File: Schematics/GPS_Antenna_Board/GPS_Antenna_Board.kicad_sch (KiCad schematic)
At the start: 26 parts, among them J1 470804001, U3 SAM-M10Q, U8 LM66100DCKR

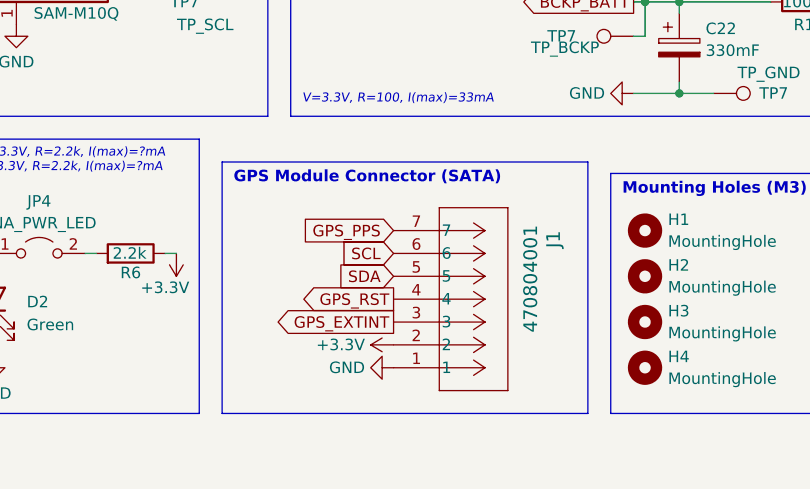
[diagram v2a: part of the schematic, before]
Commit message: Verified part numbers & made ERC pass
Also cleaned up unnecessary footprints & added bulk filtering capacitor to GPS antenna board
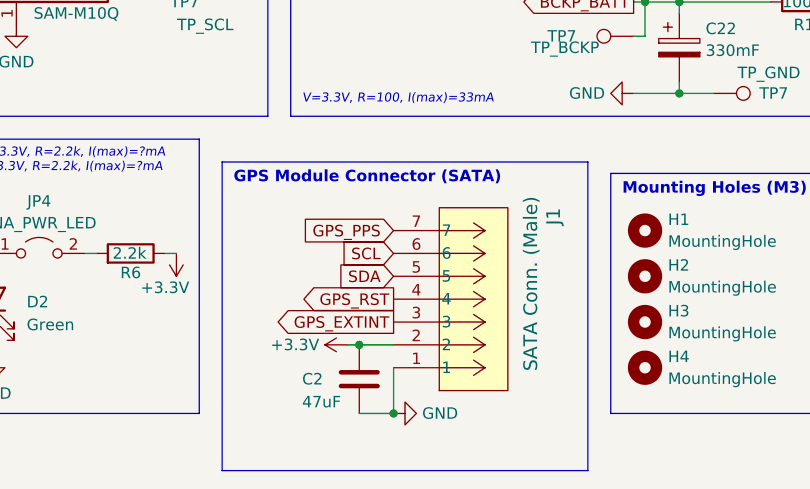
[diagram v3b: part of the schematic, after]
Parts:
- added C2: 47uF, Capacitor_SMD:C_0805_2012Metric, symbol Device:C
- J1: value 470804001 -> SATA Conn. (Male); footprint footprints:CONN_47080-4001_MOL_SATA -> CONN_47080-4001_MOL
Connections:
- net +3.3V: now also C2.1
- net GND: now also C2.2
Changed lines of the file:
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@@
   (junction (at 119.38 62.23) (diameter 0) (color 0 0 0 0)
   )
+  (junction (at 154.94 125.73) (diameter 0) (color 0 0 0 0)
+  )
   (junction (at 99.06 77.47) (diameter 0) (color 0 0 0 0)
   )
@@
   )
   (junction (at 186.69 87.63) (diameter 0) (color 0 0 0 0)
+  )
+  (junction (at 158.75 133.35) (diameter 0) (color 0 0 0 0)
   )
   (junction (at 134.62 80.01) (diameter 0) (color 0 0 0 0)
@@
     (stroke (width 0) (type default))
   )
+  (wire (pts (xy 158.75 128.27) (xy 158.75 133.35))
+    (stroke (width 0) (type default))
+  )
   (wire (pts (xy 119.38 55.88) (xy 119.38 62.23))
     (stroke (width 0) (type default))
@@
     (stroke (width 0) (type default))
   )
+  (wire (pts (xy 153.67 125.73) (xy 154.94 125.73))
+    (stroke (width 0) (type default))
+  )
   (wire (pts (xy 186.69 91.44) (xy 186.69 87.63))
     (stroke (width 0) (type default))
@@
     (stroke (width 0) (type default))
   )
+  (wire (pts (xy 154.94 125.73) (xy 158.75 125.73))
+    (stroke (width 0) (type default))
+  )
   (wire (pts (xy 129.54 82.55) (xy 134.62 82.55))
     (stroke (width 0) (type default))
@@
     (stroke (width 0) (type default))
   )
+  (wire (pts (xy 154.94 133.35) (xy 158.75 133.35))
+    (stroke (width 0) (type default))
+  )
   (wire (pts (xy 162.56 76.2) (xy 165.1 76.2))
     (stroke (width 0) (type default))
@@
     (fill (type none))
   )
-  (rectangle (start 139.7 105.41) (end 180.34 133.35)
+  (rectangle (start 139.7 105.41) (end 180.34 139.7)
     (stroke (width 0) (type default))
     (fill (type none))
@@
       (effects (font (size 1.27 1.27) italic) hide)
     )
-    (property "Datasheet" "https://www.ti.com/general/docs/suppproductinfo.tsp?distId=10&gotoUrl=https%3A%2F%2Fwww.ti.com%2Flit%2Fgpn%2flm66100" (at 185.42 74.93 0)
+    (property "Datasheet" "" (at 185.42 74.93 0)
       (effects (font (size 1.27 1.27) italic) hide)
     )
@@
     )
   )
-  (symbol (lib_id "power:+3.3V") (at 158.75 125.73 90) (unit 1)
+  (symbol (lib_id "power:+3.3V") (at 153.67 125.73 90) (unit 1)
     (in_bom yes) (on_board yes) (dnp no) (fields_autoplaced)
-    (property "Reference" "#PWR02" (at 162.56 125.73 0)
-      (effects (font (size 1.27 1.27)) hide)
-    )
-    (property "Value" "+3.3V" (at 155.575 125.73 90)
-      (effects (font (size 1.27 1.27)) (justify left))
-    )
-    (property "Footprint" "" (at 158.75 125.73 0)
-      (effects (font (size 1.27 1.27)) hide)
-    )
-    (property "Datasheet" "" (at 158.75 125.73 0)
+    (property "Reference" "#PWR02" (at 157.48 125.73 0)
+      (effects (font (size 1.27 1.27)) hide)
+    )
+    (property "Value" "+3.3V" (at 150.495 125.73 90)
+      (effects (font (size 1.27 1.27)) (justify left))
+    )
+    (property "Footprint" "" (at 153.67 125.73 0)
+      (effects (font (size 1.27 1.27)) hide)
+    )
+    (property "Datasheet" "" (at 153.67 125.73 0)
       (effects (font (size 1.27 1.27)) hide)
     )
@@
   (symbol (lib_id "CONN_47080-4001_MOL_SATA:470804001") (at 158.75 128.27 0) (mirror x) (unit 1)
     (in_bom yes) (on_board yes) (dnp no)
-    (property "Reference" "J1" (at 176.53 113.03 90)
+    (property "Reference" "J1" (at 176.53 110.49 90)
       (effects (font (size 1.524 1.524)) (justify left))
     )
-    (property "Value" "470804001" (at 173.99 112.395 90)
+    (property "Value" "SATA Conn. (Male)" (at 173.99 109.22 90)
       (effects (font (size 1.524 1.524)) (justify left))
     )
-    (property "Footprint" "footprints:CONN_47080-4001_MOL_SATA" (at 158.75 128.27 0)
+    (property "Footprint" "CONN_47080-4001_MOL" (at 158.75 128.27 0)
       (effects (font (size 1.27 1.27) italic) hide)
     )
@@
     )
   )
-  (symbol (lib_id "power:GND") (at 158.75 128.27 270) (unit 1)
+  (symbol (lib_id "power:GND") (at 158.75 133.35 90) (unit 1)
     (in_bom yes) (on_board yes) (dnp no) (fields_autoplaced)
-    (property "Reference" "#PWR01" (at 152.4 128.27 0)
-      (effects (font (size 1.27 1.27)) hide)
-    )
-    (property "Value" "GND" (at 155.5751 128.27 90)
+    (property "Reference" "#PWR01" (at 165.1 133.35 0)
+      (effects (font (size 1.27 1.27)) hide)
+    )
+    (property "Value" "GND" (at 161.925 133.35 90)
       (effects (font (size 1.27 1.27)) (justify right))
     )
-    (property "Footprint" "" (at 158.75 128.27 0)
-      (effects (font (size 1.27 1.27)) hide)
-    )
-    (property "Datasheet" "" (at 158.75 128.27 0)
+    (property "Footprint" "" (at 158.75 133.35 0)
+      (effects (font (size 1.27 1.27)) hide)
+    )
+    (property "Datasheet" "" (at 158.75 133.35 0)
       (effects (font (size 1.27 1.27)) hide)
     )
@@
         )
       )
+    )
+  )
+  (symbol (lib_id "Device:C") (at 154.94 129.54 0) (unit 1)
+    (in_bom yes) (on_board yes) (dnp no)
+    (property "Reference" "C2" (at 148.59 129.54 0)
+      (effects (font (size 1.27 1.27)) (justify left))
+    )
+    (property "Value" "47uF" (at 148.59 132.08 0)
+      (effects (font (size 1.27 1.27)) (justify left))
+    )
+    (property "Footprint" "Capacitor_SMD:C_0805_2012Metric" (at 155.9052 133.35 0)
+      (effects (font (size 1.27 1.27)) hide)
+    )
+    (property "Datasheet" "~" (at 154.94 129.54 0)
+      (effects (font (size 1.27 1.27)) hide)
+    )
+    (property "LCSC" "C16780" (at 151.511 129.54 90)
+      (effects (font (size 1.27 1.27)) hide)
+    )
+    (pin "1")
+    (pin "2")
+    (instances
+      (project "CANBUSALL"
+        (path "/93bab7a2-0f5f-4ce1-a774-248550723259"
+          (reference "C2") (unit 1)
+        )
+      )
+      (project "canbusv1"
+        (path "/acb9ae9d-257e-47aa-b94e-3fc0ebc9a75c"
+          (reference "C1") (unit 1)
+        )
+      )
+      (project "Communications_Module"
+        (path "/ace06731-9b48-45c3-868d-c65fed1a8f9b"
+          (reference "C19") (unit 1)
+        )
+      )
+      (project "GPS_Module"
+        (path "/c9a01778-8bed-4fe7-bd5a-975b80c0ed6a"
+          (reference "C12") (unit 1)
+        )
+      )
+      (project "GPS_Antenna_Board"
+        (path "/f34e830a-ca26-47f3-b516-e4270044d2c1"
+          (reference "C5") (unit 1)
+        )
+      )

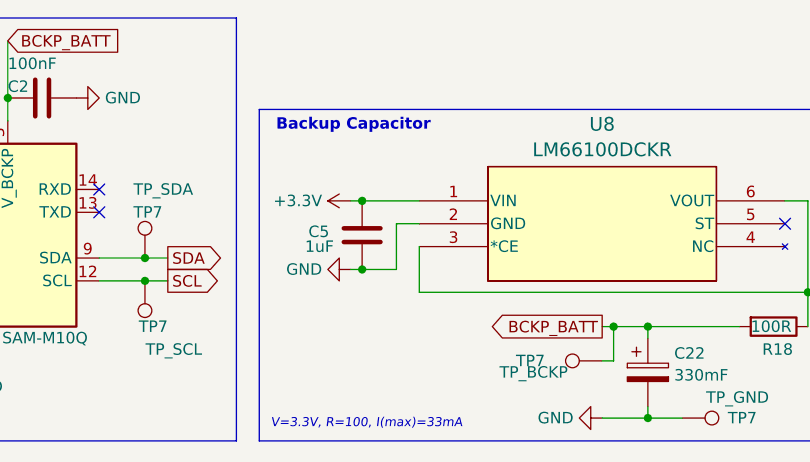
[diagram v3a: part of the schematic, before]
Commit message: Add silkscreen & final PCB adjustments
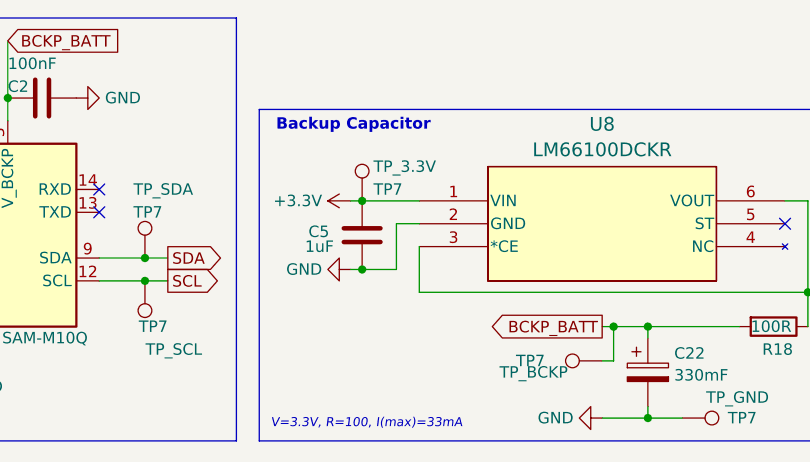
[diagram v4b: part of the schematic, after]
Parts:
- added TP7: TP_3.3V, TestPoint:TestPoint_Pad_1.5x1.5mm, symbol Connector:TestPoint
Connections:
- net +3.3V: now also TP7.1
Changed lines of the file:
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@@
+    )
+  )
+  (symbol (lib_id "Connector:TestPoint") (at 158.75 73.66 0) (unit 1)
+    (in_bom no) (on_board yes) (dnp no)
+    (property "Reference" "TP7" (at 160.02 72.39 0)
+      (effects (font (size 1.27 1.27)) (justify left))
+    )
+    (property "Value" "TP_3.3V" (at 160.02 69.85 0)
+      (effects (font (size 1.27 1.27)) (justify left))
+    )
+    (property "Footprint" "TestPoint:TestPoint_Pad_1.5x1.5mm" (at 163.83 73.66 0)
+      (effects (font (size 1.27 1.27)) hide)
+    )
+    (property "Datasheet" "~" (at 163.83 73.66 0)
+      (effects (font (size 1.27 1.27)) hide)
+    )
+    (pin "1")
+    (instances
+      (project "Communications_Module"
+        (path "/ace06731-9b48-45c3-868d-c65fed1a8f9b"
+          (reference "TP7") (unit 1)
+        )
+      )
+      (project "GPS_Module"
+        (path "/c9a01778-8bed-4fe7-bd5a-975b80c0ed6a"
+          (reference "TP11") (unit 1)
+        )
+      )
+      (project "GPS_Antenna_Board"
+        (path "/f34e830a-ca26-47f3-b516-e4270044d2c1"
+          (reference "TP8") (unit 1)
+        )
+      )
     )
   )

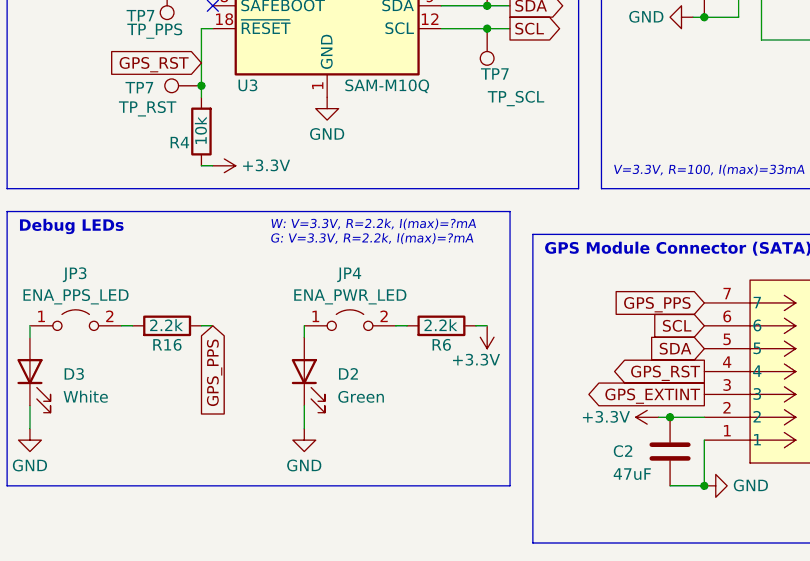
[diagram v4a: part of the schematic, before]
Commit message: Updated Debug/PPS/Power LED resistors
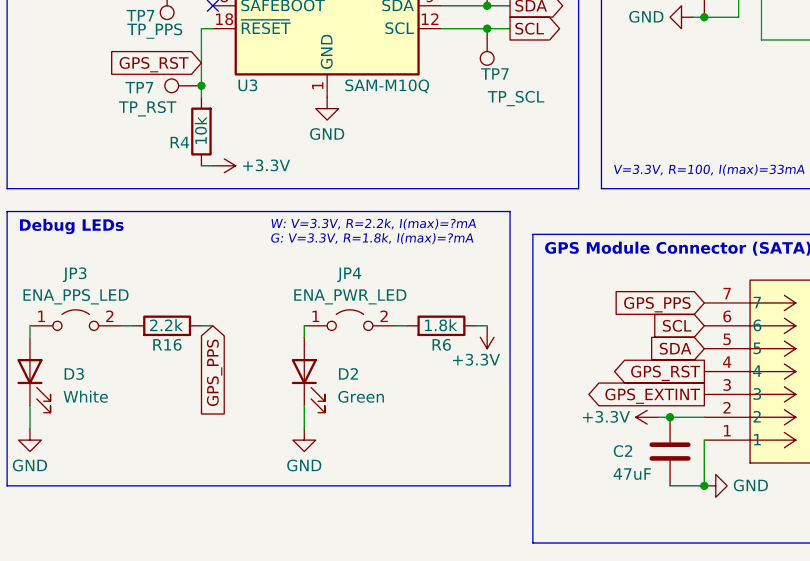
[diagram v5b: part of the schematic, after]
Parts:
- J1: footprint CONN_47080-4001_MOL -> footprints:CONN_47080-4001_MOL_SATA
- R6: value 2.2k -> 1.8k; LCSC C4190 -> C4177
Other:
- note added: "W: V=3.3V, R=2.2k, I(max)=?mA G: V=3.3V, R=1.8k, I(max)=?mA"
- note removed: "W: V=3.3V, R=2.2k, I(max)=?mA G: V=3.3V, R=2.2k, I(max)=?mA"
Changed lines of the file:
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@@
     (fill (type none))
   )
-  (text "W: V=3.3V, R=2.2k, I(max)=?mA\nG: V=3.3V, R=2.2k, I(max)=?mA"
+  (text "W: V=3.3V, R=2.2k, I(max)=?mA\nG: V=3.3V, R=1.8k, I(max)=?mA"
     (at 110.49 106.68 0)
     (effects (font (size 1 1) italic) (justify left bottom))
@@
       (effects (font (size 1.27 1.27)))
     )
-    (property "Value" "2.2k" (at 129.413 115.57 90)
+    (property "Value" "1.8k" (at 129.413 115.57 90)
       (effects (font (size 1.27 1.27)))
     )
@@
       (effects (font (size 1.27 1.27)) hide)
     )
-    (property "LCSC" "C4190" (at 129.413 113.665 90)
+    (property "LCSC" "C4177" (at 129.413 113.665 90)
       (effects (font (size 1.27 1.27)) hide)
     )
@@
       (effects (font (size 1.524 1.524)) (justify left))
     )
-    (property "Footprint" "CONN_47080-4001_MOL" (at 158.75 128.27 0)
+    (property "Footprint" "footprints:CONN_47080-4001_MOL_SATA" (at 158.75 128.27 0)
       (effects (font (size 1.27 1.27) italic) hide)
     )

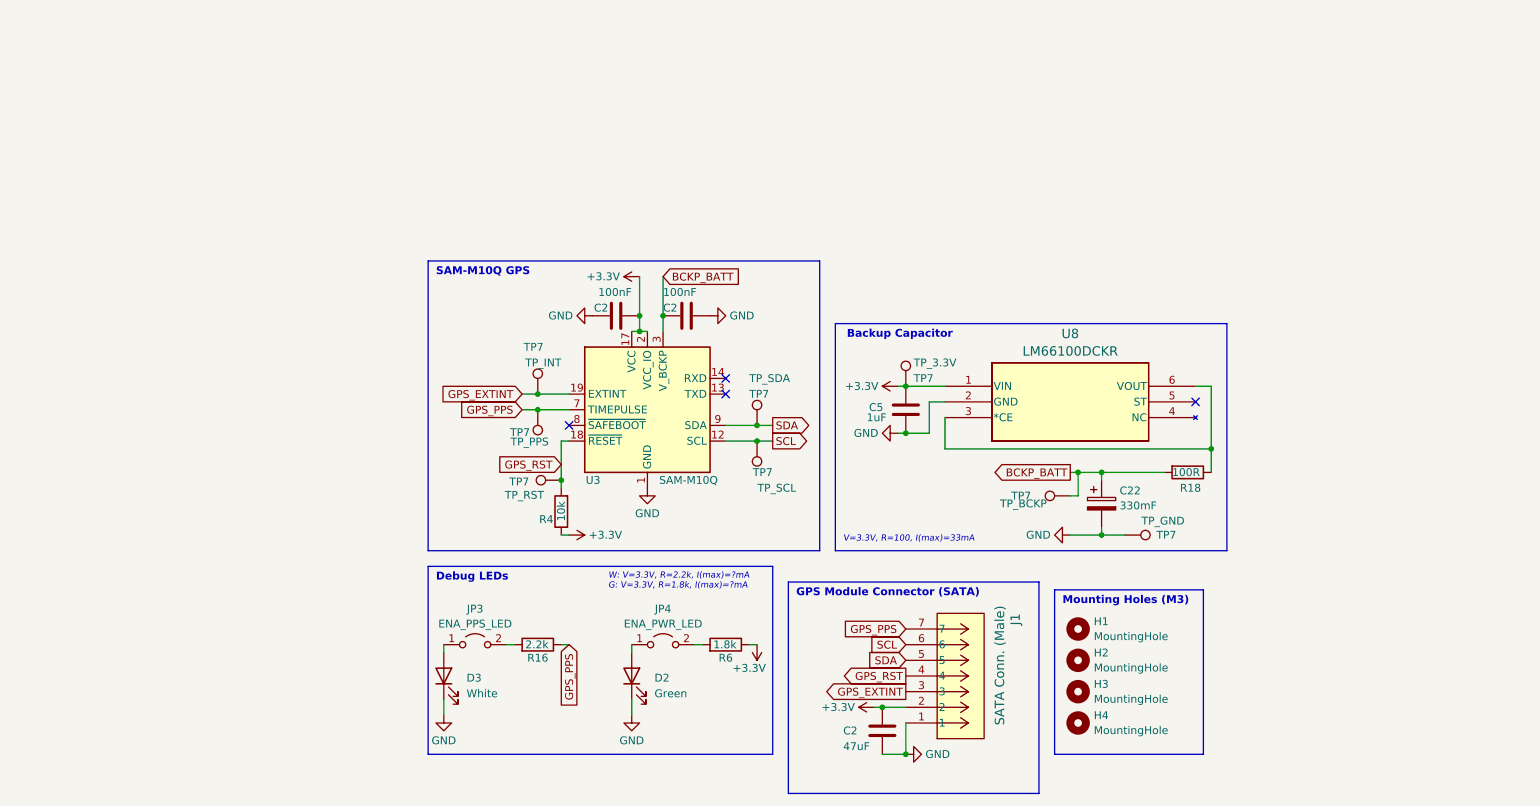
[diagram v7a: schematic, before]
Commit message: Fixed SATA pinout + Dimmed power LED
Most SATA cables short pins 1,4,7 together as GND. For Rev 1.0, this meant the PPS, RESET, and GND pins were all tied together, effectively bricking the GPS.

This has been revised by disconnecting pins 4 & 7, discarding the PPS signal entirely and then sharing pin 3 for EITHER the reset signal or external interrupt signal. Updated board routing as needed.

Also quickly tweaked the power LED resistor so the LED is dimmer. (1.8k to 3.3k)
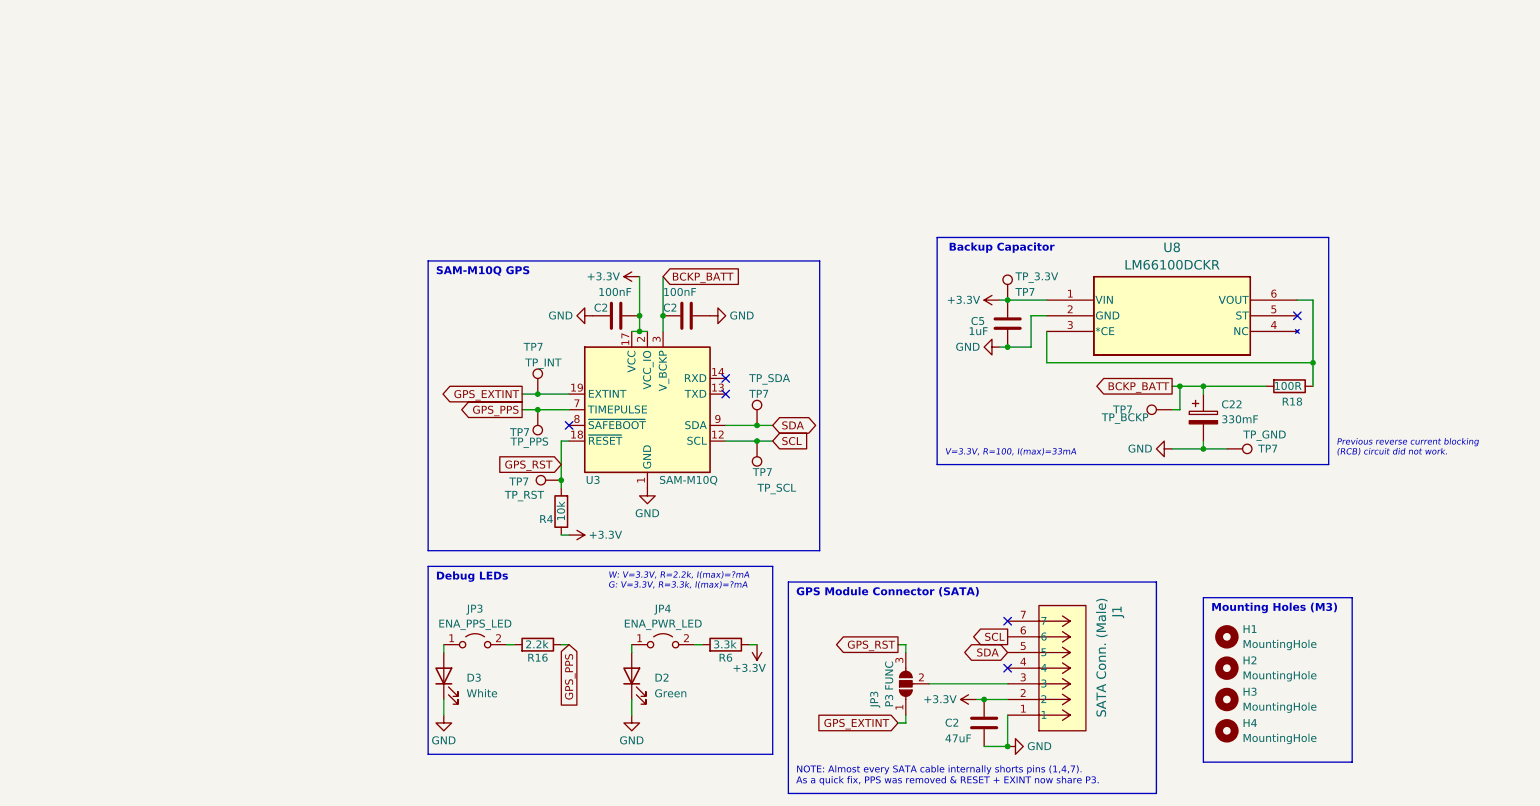
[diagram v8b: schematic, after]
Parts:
- added JP3: P3 FUNC, Jumper:SolderJumper-3_P1.3mm_Open_RoundedPad1.0x1.5mm, symbol Jumper:SolderJumper_3_Open
- R6: value 1.8k -> 3.3k; LCSC C4177 -> C22978
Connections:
- net GPS_EXTINT: now also JP3.1 (A); no longer J1.3
- net GPS_PPS: no longer J1.7
- net GPS_RST: now also JP3.3 (B); no longer J1.4
- new net: J1.3, JP3.2 (C)
- no-connect marks 4 -> 6
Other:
- note added: "NOTE: Almost every SATA cable internally shorts pins (1,4,7). As a quick fix, PPS was removed & RESET + EXINT now share P3."
- note added: "Previous reverse current blocking (RCB) circuit did not work."
- note added: "W: V=3.3V, R=2.2k, I(max)=?mA G: V=3.3V, R=3.3k, I(max)=?mA"
- note removed: "W: V=3.3V, R=2.2k, I(max)=?mA G: V=3.3V, R=1.8k, I(max)=?mA"
- moved on the sheet: C2, C22, C5, H1, H2, H3, H4, J1, R18, TP7, U8
